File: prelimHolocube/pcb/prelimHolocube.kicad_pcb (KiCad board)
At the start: 2 copper layers, 28.2 x 51.4 mm, 43 parts

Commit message: finish pcb
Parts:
- removed C25, C27: 1uF, Capacitor_THT:CP_Radial_D5.0mm_P2.50mm
- removed C26, C28, C29, C30: 4.7uF, Capacitor_THT:CP_Radial_D4.0mm_P2.00mm
- removed the U4 at (127.2, 81.5)
- added C16: 4.7uF, Capacitor_THT:CP_Radial_D4.0mm_P2.00mm, B.Cu at (137.2, 144.9)
- added C17: 4.7uF, Capacitor_THT:CP_Radial_D4.0mm_P2.00mm, B.Cu at (193.0, 59.5)
- added C18: 4.7uF, Capacitor_THT:CP_Radial_D4.0mm_P2.00mm, B.Cu at (143.2, 144.9)
- added C7: 1uF, Capacitor_THT:CP_Radial_D5.0mm_P2.50mm, B.Cu at (131.0, 59.6)
- added C8: 4.7uF, Capacitor_THT:CP_Radial_D4.0mm_P2.00mm, B.Cu at (137.5, 59.6)
- added C9: 4.7uF, Capacitor_THT:CP_Radial_D4.0mm_P2.00mm, B.Cu at (144.1, 59.6)
- added R6: 1M, Resistor_THT:R_Axial_DIN0207_L6.3mm_D2.5mm_P7.62mm_Horizontal, B.Cu at (171.7, 108.4)
- added U3: ~, transparent_oled_display:surenoo-1.12in-128x128, F.Cu at (135.8, 76.2)
- C15: value 4.7uF -> 1uF; footprint Capacitor_THT:CP_Radial_D4.0mm_P2.00mm -> Capacitor_THT:CP_Radial_D5.0mm_P2.50mm
- U10: moved to B.Cu
- moved U5 88.0 mm to (185.8, 76.2), turned to -90 degrees
- moved C10 82.7 mm to (156.7, 59.9)
- moved C13 80.3 mm to (181.2, 59.5)
- moved U2 75.8 mm to (186.8, 102.2), turned to 180 degrees
- moved R3 75.4 mm to (115.1, 98.3), turned to -90 degrees
- moved U10 69.0 mm to (106.7, 144.9), turned to 180 degrees
- moved C11 62.7 mm to (162.8, 60.0)
- moved C14 59.0 mm to (187.3, 59.5)
- moved U8 58.9 mm to (185.8, 128.2), turned to 90 degrees
- moved C4 58.2 mm to (204.8, 96.1)
- moved U7 57.5 mm to (160.8, 128.2), turned to 90 degrees
- moved U4 57.4 mm to (160.8, 76.2), turned to -90 degrees
- moved U1 56.2 mm to (134.8, 102.2)
- moved U9 52.2 mm to (106.7, 102.2)
- moved C12 51.7 mm to (168.9, 60.1)
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- renumbered U3 to U4
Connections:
- C15 pad 1: Net-(U4-VCOMH) (its old number) -> GND
- C15 pad 2: GND -> +3.3V
- C23 pad 1: Net-(U5-VCOMH) -> Net-(U7-VCOMH)
- C24 pad 1: Net-(U7-VCOMH) -> Net-(U8-VCOMH)
- R7 pad 1: Net-(U5-IREF) -> Net-(U6-IREF)
- R9 pad 1: Net-(U6-IREF) -> Net-(U8-IREF)
- U4 pad 4: A03 -> A04
- U4 pad 6: CS3 -> CS4
- U4 pad 7: Net-(U3-IREF) -> Net-(U4-IREF)
- U6 pad 4: A06 -> A07
- U6 pad 6: CS6 -> CS7
- U7 pad 4: A07 -> A06
- U7 pad 6: CS7 -> CS6
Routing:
- net GND: track 0.00 -> 522.7 mm, vias 0 -> 11
- net +12V: track 0.00 -> 423.0 mm, vias 0 -> 17
- net +3.3V: track 0.00 -> 318.1 mm, vias 0 -> 13
- net SCL: track 0.00 -> 274.3 mm, vias 0 -> 9
- net SI: track 0.00 -> 257.7 mm, vias 0 -> 6
- net RES: track 0.00 -> 244.7 mm, vias 0 -> 8
- net CS2: track 0.00 -> 217.6 mm, vias 0 -> 1
- net A08: track 0.00 -> 210.6 mm
- net A05: track 0.00 -> 139.9 mm, vias 0 -> 2
- net CS5: track 0.00 -> 139.6 mm, vias 0 -> 1
- net CS6: track 0.00 -> 129.9 mm, vias 0 -> 1
- net CS8: track 0.00 -> 118.5 mm, vias 0 -> 2
- net A04: track 0.00 -> 117.5 mm, vias 0 -> 2
- net CS7: track 0.00 -> 112.3 mm
- net CS4: track 0.00 -> 107.6 mm, vias 0 -> 1
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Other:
- board size 28.2 x 51.4 mm -> 120 x 100 mm
- board text added: "4.7uF = big capacitor footprint 1uF = small capacitor footprint"
- board text removed: "1M ^ 10k v"
- board text removed: "4.7uF ^ 1uF v"

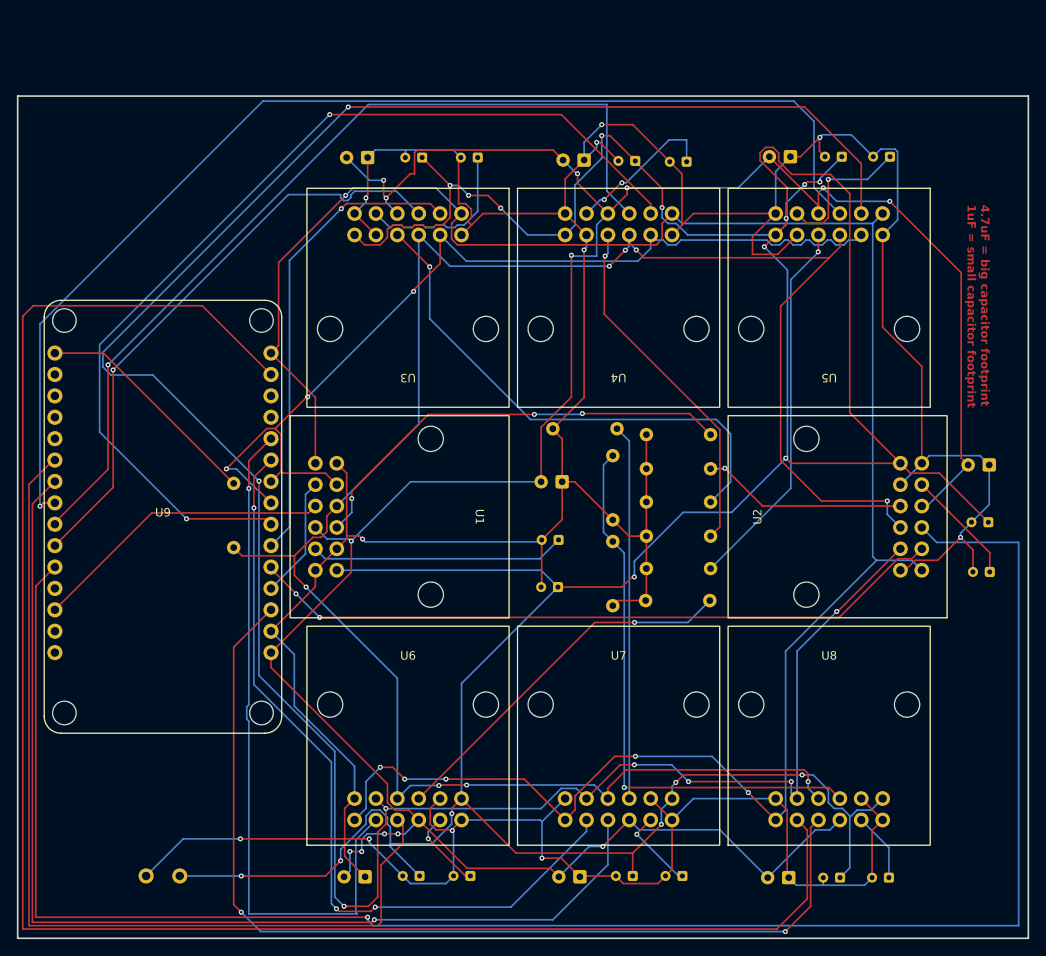
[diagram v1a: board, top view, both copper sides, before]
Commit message: add cad model and mounting holes
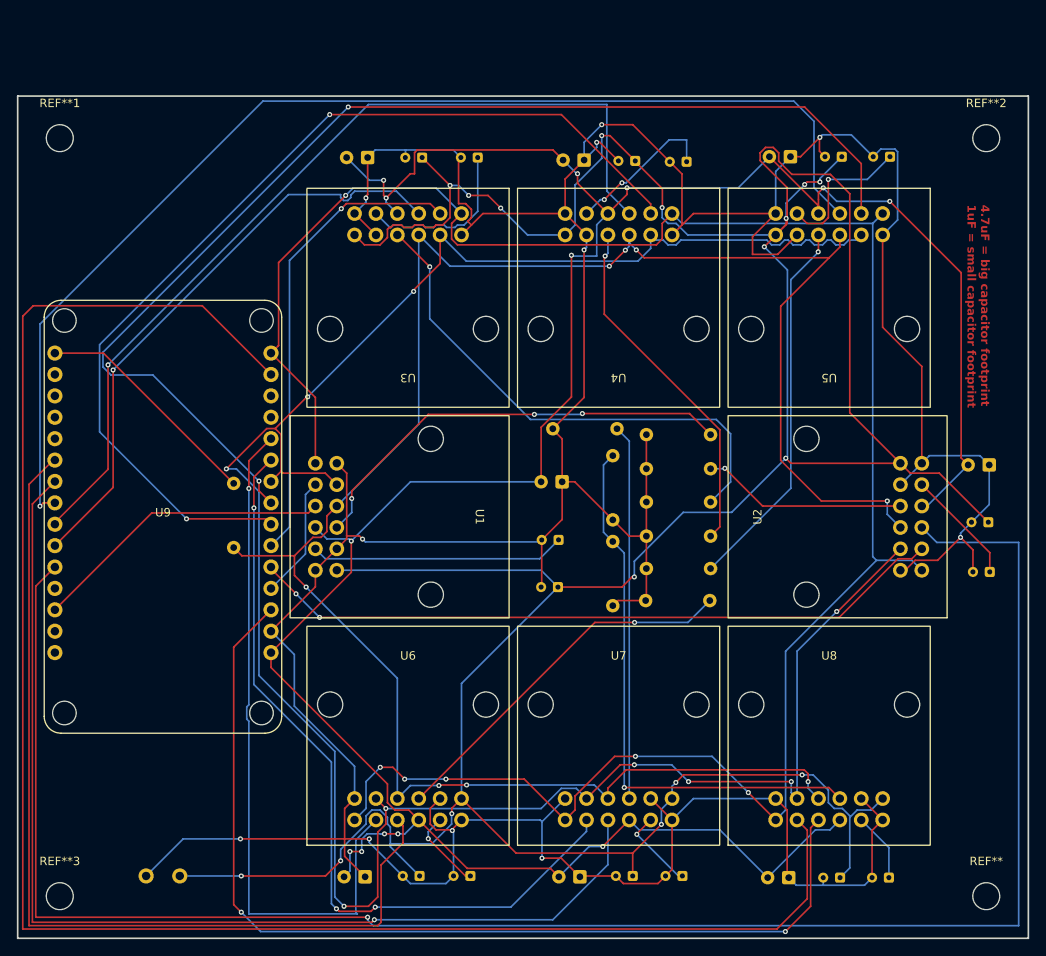
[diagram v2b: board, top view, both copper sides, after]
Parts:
- added REF**: MountingHole_3.2mm_M3, MountingHole:MountingHole_3.2mm_M3, F.Cu at (204.5, 147.3)
- added REF**1: MountingHole_3.2mm_M3, MountingHole:MountingHole_3.2mm_M3, F.Cu at (94.5, 57.3)
- added REF**2: MountingHole_3.2mm_M3, MountingHole:MountingHole_3.2mm_M3, F.Cu at (204.5, 57.3)
- added REF**3: MountingHole_3.2mm_M3, MountingHole:MountingHole_3.2mm_M3, F.Cu at (94.5, 147.3)

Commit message: switched to holo's prelimHolocube using this as a reference, deleted tracks to flip footprint, need to reroute
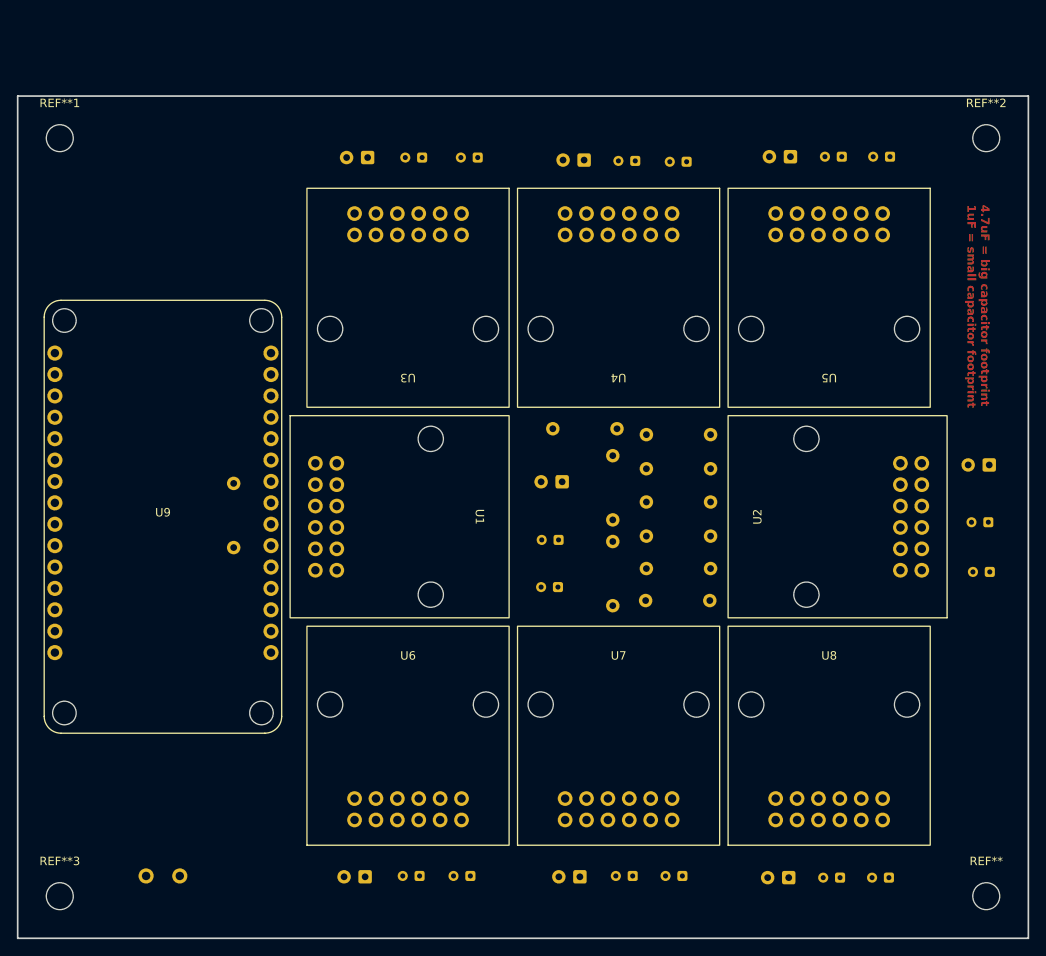
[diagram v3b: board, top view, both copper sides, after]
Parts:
- C10, C13, C15, C19, C2, C21, C4, C7: value 1uF -> 1uF ceramic
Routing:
- net GND: track 522.7 -> 0.00 mm, vias 11 -> 0
- net +12V: track 423.0 -> 0.00 mm, vias 17 -> 0
- net +3.3V: track 318.1 -> 0.00 mm, vias 13 -> 0
- net SCL: track 274.3 -> 0.00 mm, vias 9 -> 0
- net SI: track 257.7 -> 0.00 mm, vias 6 -> 0
- net RES: track 244.7 -> 0.00 mm, vias 8 -> 0
- net CS2: track 217.6 -> 0.00 mm, vias 1 -> 0
- net A08: track 210.6 -> 0.00 mm
- net A05: track 139.9 -> 0.00 mm, vias 2 -> 0
- net CS5: track 139.6 -> 0.00 mm, vias 1 -> 0
- net CS6: track 129.9 -> 0.00 mm, vias 1 -> 0
- net CS8: track 118.5 -> 0.00 mm, vias 2 -> 0
- net A04: track 117.5 -> 0.00 mm, vias 2 -> 0
- net CS7: track 112.3 -> 0.00 mm
- net CS4: track 107.6 -> 0.00 mm, vias 1 -> 0
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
